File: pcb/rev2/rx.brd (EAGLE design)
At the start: 19 x 38 mm, 34 parts, among them Y1 CRYSTAL-26MHZSMD-3.2X2.5

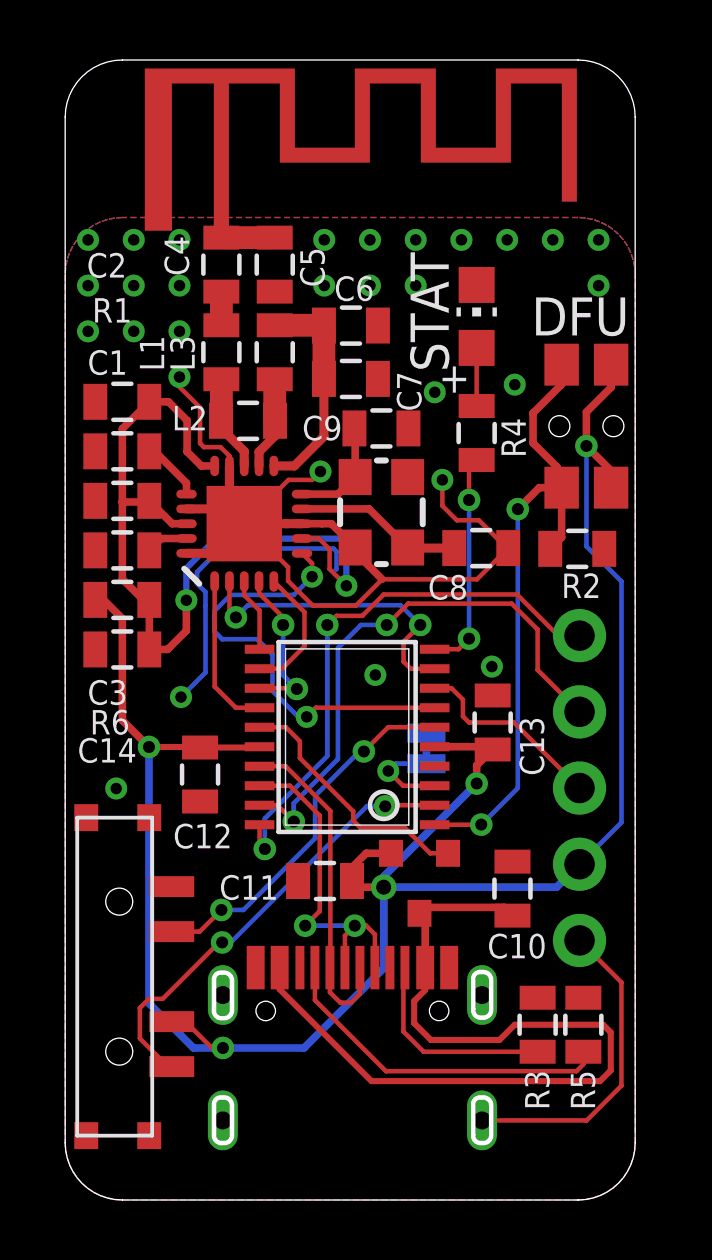
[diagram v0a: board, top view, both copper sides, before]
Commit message: added more power filtering, added RX interrupt
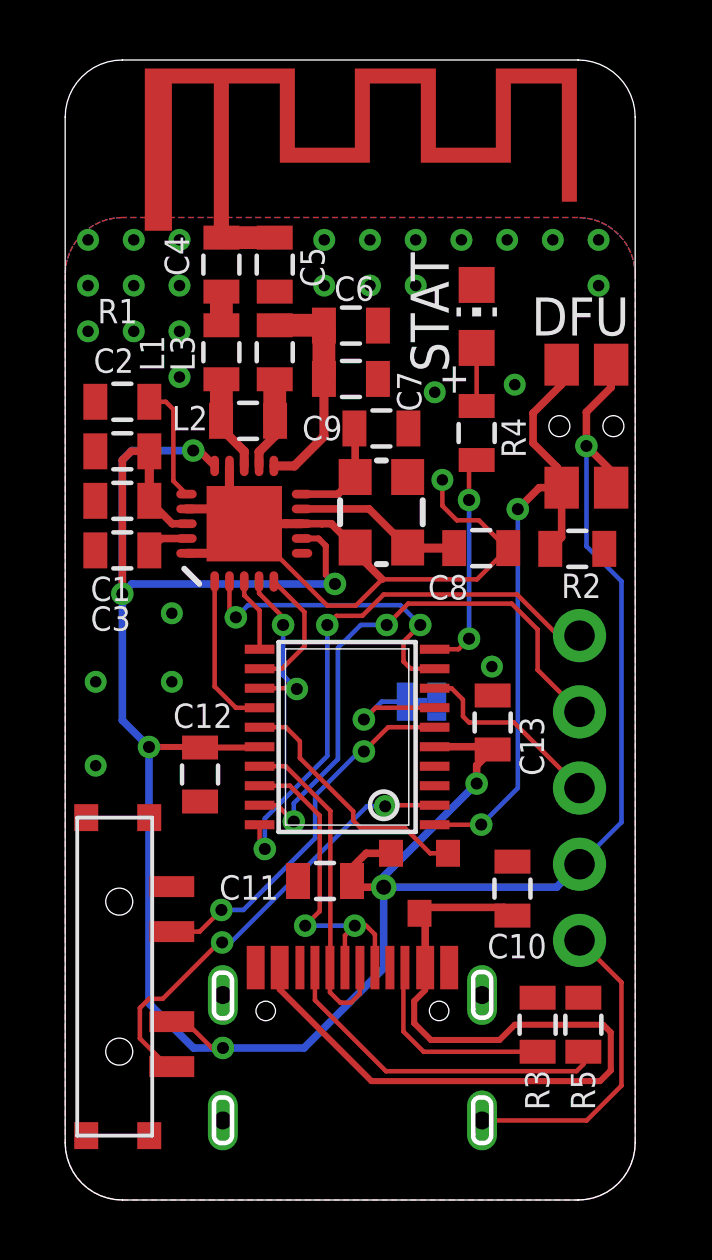
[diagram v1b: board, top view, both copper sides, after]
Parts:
- removed C14: 100nF, clock:0805
- removed R6: 1 Ohm, joyAnalog:0805
- moved C2 1.65 mm to (1.91, 25.0)
- moved R1 1.65 mm to (1.91, 26.6)
- moved SJ1 1.57 mm to (11.9, 16.6), turned to 0 degrees
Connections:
- removed net N$28: C1.1, C14.1, C2.1, R6.2, U$3.15, U$3.18, U$3.7
- removed net N$30: U$2.7, U$3.6
- net +3V3: now also C1.1, C2.1, U$3.15, U$3.18, U$3.7; no longer R6.1
- net GND: no longer C14.2
- net N$19: now also U$2.7; no longer U$2.3
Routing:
- net N$28: track 28.6 -> 0.00 mm, vias 2 -> 0
- net +3V3: track 70.2 -> 95.9 mm, vias 5 -> 8
- net GND: track 63.0 -> 45.6 mm
- net N$30: track 14.7 -> 0.00 mm, vias 2 -> 0
- net N$2: track 2.04 -> 3.91 mm
- net N$19: track 3.12 -> 4.18 mm
